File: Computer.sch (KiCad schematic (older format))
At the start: 35 parts, among them J1 DB9, J2 Screw_Terminal_1x04, U1 8284, U10 74LS04, U11 7400, U12 8259, U2 LM2931AZ-5.0, U3 8088, U4 74LS04, U5 28C256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

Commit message: Update to revision A
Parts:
- removed unit 2 of U4
- removed unit 3 of U4
- removed unit 4 of U4
- removed unit 5 of U4
- removed U8: 7400, Housings_DIP:DIP-14_W7.62mm, symbol 7400
- added R16, R17, R4, R5: 10k, Resistors_THT:R_Axial_DIN0204_L3.6mm_D1.6mm_P7.62mm_Horizontal, symbol R
- added unit 6 of U10
- added unit 5 of U10
- added U13, U8: 74LS138, Housings_DIP:DIP-16_W7.62mm, symbol 74LS138
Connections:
- net A0: now also U13.1 (A0), U13.3 (A2)
- net A17: now also U8.1 (A0)
- net A18: now also U8.2 (A1)
- net A19: now also U8.3 (A2)
- net A4: now also U13.2 (A1)
- net GND: now also R16.1, R5.1, U10.7 (GND), U10.7 (GND), U13.8 (GND), U8.8 (GND)
- net IO/M: now also U10.13, U8.5 (E2); no longer U10.3, U10.5, U10.9, U3.32 (~RD~), U5.22 (OE), U6.22 (OE), U7.21 (~RD~)
- net VCC: now also U10.14 (VCC), U10.14 (VCC), U13.16 (VCC), U8.16 (VCC)
- net Vcc: now also R17.2, R4.1
- net WR: now also U10.11
- net at U5.20 (CS): now also U8.7 (O7); no longer U5.27 (WE)
- net at U6.20 (CS): now also U8.15 (O0)
- net at U7.14 (~CS2~): now also U13.15 (O0)
- net at R11.1: now also U5.27 (WE)
- new net: U10.8, U7.21 (~RD~)
- new net: U12.1 (~CS~), U13.14 (O1)
- new net: U10.10, U12.3 (~WR~)
- new net: R5.2, U8.4 (E1)
- new net: R4.2, U8.6 (E3)
- new net: U10.12, U13.4 (E1)
- new net: R16.2, U13.5 (E2)
- new net: R17.1, U13.6 (E3)
- new net RD: U10.3, U10.5, U10.9, U12.2 (~RD~), U3.32 (~RD~), U5.22 (OE), U6.22 (OE)
- no-connect marks 32 -> 44

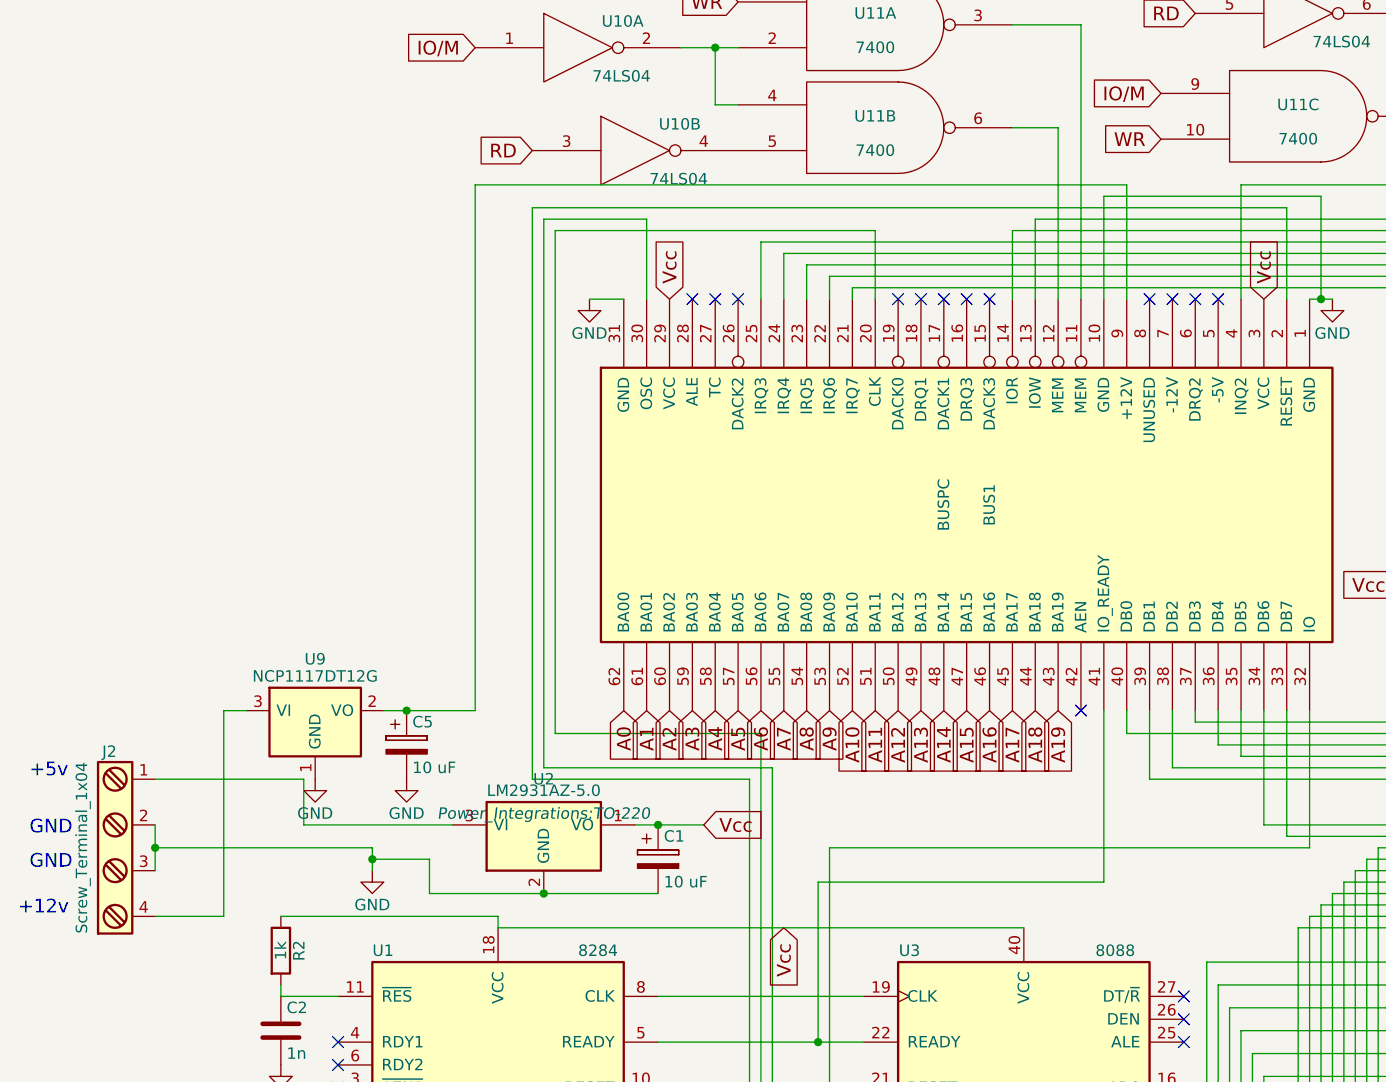
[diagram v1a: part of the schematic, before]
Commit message: Add -12v and -5v rails
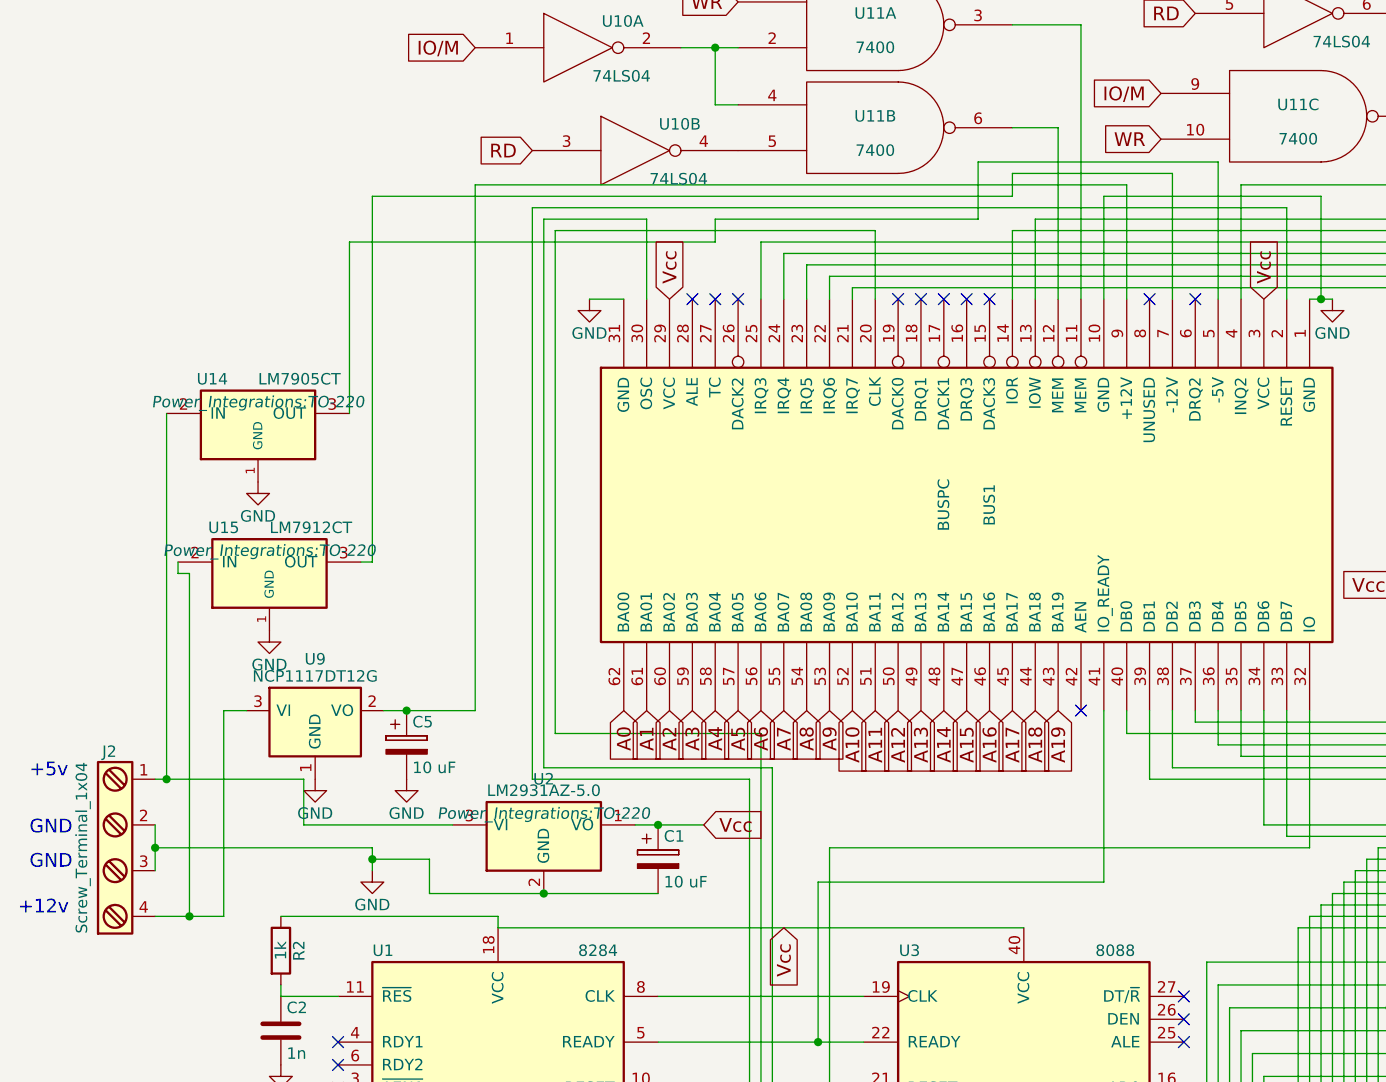
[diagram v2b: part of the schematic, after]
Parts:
- added U14: LM7905CT, Power_Integrations:TO-220, symbol LM7905CT
- added U15: LM7912CT, Power_Integrations:TO-220, symbol LM7912CT
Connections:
- net GND: now also U14.1 (GND), U15.1 (GND)
- net at J2.1, U2.3 (VI): now also U14.2 (IN)
- net at BUS1.5 (-5V): now also U14.3 (OUT)
- net at BUS1.7 (-12V): now also U15.3 (OUT)
- net at J2.4, U9.3 (VI): now also U15.2 (IN)
- no-connect marks 44 -> 42
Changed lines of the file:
@@
 $EndDescr
 $Comp
-L GND #PWR4
+L GND #PWR6
 U 1 1 5887F82B
 P 2300 4700
-F 0 "#PWR4" H 2300 4450 50  0001 C CNN
+F 0 "#PWR6" H 2300 4450 50  0001 C CNN
 F 1 "GND" H 2300 4550 50  0000 C CNN
 F 2 "" H 2300 4700 50  0000 C CNN
@@
 $EndComp
 $Comp
-L GND #PWR9
+L GND #PWR11
 U 1 1 58881BF2
 P 4000 8700
-F 0 "#PWR9" H 4000 8450 50  0001 C CNN
+F 0 "#PWR11" H 4000 8450 50  0001 C CNN
 F 1 "GND" H 4000 8550 50  0000 C CNN
 F 2 "" H 4000 8700 50  0000 C CNN
@@
 $EndComp
 $Comp
-L GND #PWR2
+L GND #PWR4
 U 1 1 58888005
 P 1900 5550
-F 0 "#PWR2" H 1900 5300 50  0001 C CNN
+F 0 "#PWR4" H 1900 5300 50  0001 C CNN
 F 1 "GND" H 1900 5400 50  0000 C CNN
 F 2 "" H 1900 5550 50  0000 C CNN
@@
 $EndComp
 $Comp
-L GND #PWR14
+L GND #PWR16
 U 1 1 588F1D61
 P 10100 8150
-F 0 "#PWR14" H 10100 7900 50  0001 C CNN
+F 0 "#PWR16" H 10100 7900 50  0001 C CNN
 F 1 "GND" H 10100 8000 50  0000 C CNN
 F 2 "" H 10100 8150 50  0000 C CNN
@@
 $EndComp
 $Comp
-L GND #PWR12
+L GND #PWR14
 U 1 1 588F745E
 P 8950 8300
-F 0 "#PWR12" H 8950 8050 50  0001 C CNN
+F 0 "#PWR14" H 8950 8050 50  0001 C CNN
 F 1 "GND" H 8950 8150 50  0000 C CNN
 F 2 "" H 8950 8300 50  0000 C CNN
@@
 $EndComp
 $Comp
-L GND #PWR7
+L GND #PWR9
 U 1 1 588FA3EB
 P 3000 10650
-F 0 "#PWR7" H 3000 10400 50  0001 C CNN
+F 0 "#PWR9" H 3000 10400 50  0001 C CNN
 F 1 "GND" H 3000 10500 50  0000 C CNN
 F 2 "" H 3000 10650 50  0000 C CNN
@@
 $EndComp
 $Comp
-L GND #PWR6
+L GND #PWR8
 U 1 1 588FA459
 P 2700 10650
-F 0 "#PWR6" H 2700 10400 50  0001 C CNN
+F 0 "#PWR8" H 2700 10400 50  0001 C CNN
 F 1 "GND" H 2700 10500 50  0000 C CNN
 F 2 "" H 2700 10650 50  0000 C CNN
@@
 IRQ0
 $Comp
-L GND #PWR13
+L GND #PWR15
 U 1 1 58A2012A
 P 9000 3450
-F 0 "#PWR13" H 9000 3200 50  0001 C CNN
+F 0 "#PWR15" H 9000 3200 50  0001 C CNN
 F 1 "GND" H 9000 3300 50  0000 C CNN
 F 2 "" H 9000 3450 50  0000 C CNN
@@
 NoConn ~ 5700 2200
 $Comp
-L GND #PWR11
+L GND #PWR13
 U 1 1 58A30571
 P 6500 2200
-F 0 "#PWR11" H 6500 1950 50  0001 C CNN
+F 0 "#PWR13" H 6500 1950 50  0001 C CNN
 F 1 "GND" H 6500 2050 50  0000 C CNN
 F 2 "" H 6500 2200 50  0000 C CNN
@@
 $EndComp
 $Comp
-L GND #PWR8
+L GND #PWR10
 U 1 1 58A305FA
 P 3250 2200
-F 0 "#PWR8" H 3250 1950 50  0001 C CNN
+F 0 "#PWR10" H 3250 1950 50  0001 C CNN
 F 1 "GND" H 3250 2050 50  0000 C CNN
 F 2 "" H 3250 2200 50  0000 C CNN
@@
 +12v
 $Comp
-L GND #PWR3
+L GND #PWR5
 U 1 1 58A3B81F
 P 2050 4300
-F 0 "#PWR3" H 2050 4050 50  0001 C CNN
+F 0 "#PWR5" H 2050 4050 50  0001 C CNN
 F 1 "GND" H 2050 4150 50  0000 C CNN
 F 2 "" H 2050 4300 50  0000 C CNN
@@
 $EndComp
 $Comp
-L GND #PWR5
+L GND #PWR7
 U 1 1 58A3B97D
 P 2450 4300
-F 0 "#PWR5" H 2450 4050 50  0001 C CNN
+F 0 "#PWR7" H 2450 4050 50  0001 C CNN
 F 1 "GND" H 2450 4150 50  0000 C CNN
 F 2 "" H 2450 4300 50  0000 C CNN
@@
 	1    0    0    -1
 $EndComp
-NoConn ~ 5800 2200
-NoConn ~ 6000 2200
 NoConn ~ 5900 2200
 NoConn ~ 5000 2200
@@
 IO/M
 $Comp
-L GND #PWR10
+L GND #PWR12
 U 1 1 58C8EE59
 P 4150 10000
-F 0 "#PWR10" H 4150 9750 50  0001 C CNN
+F 0 "#PWR12" H 4150 9750 50  0001 C CNN
 F 1 "GND" H 4150 9850 50  0000 C CNN
 F 2 "" H 4150 10000 50  0000 C CNN
@@
 $EndComp
 $Comp
-L GND #PWR15
+L GND #PWR17
 U 1 1 58C92558
 P 10450 4100
-F 0 "#PWR15" H 10450 3850 50  0001 C CNN
+F 0 "#PWR17" H 10450 3850 50  0001 C CNN
 F 1 "GND" H 10450 3950 50  0000 C CNN
 F 2 "" H 10450 4100 50  0000 C CNN
@@
 Text GLabel 8300 4050 3    60   Input ~ 0
 RD
+Wire Wire Line
+	1500 4900 1500 3400
+Wire Wire Line
+	1500 3400 1450 3400
+Wire Wire Line
+	1450 3400 1450 3350
+Connection ~ 1500 4900
+$Comp
+L GND #PWR3
+U 1 1 58C76930
+P 1850 3650
+F 0 "#PWR3" H 1850 3400 50  0001 C CNN
+F 1 "GND" H 1850 3500 50  0000 C CNN
+F 2 "" H 1850 3650 50  0000 C CNN
+F 3 "" H 1850 3650 50  0000 C CNN
+	1    1850 3650
+	1    0    0    -1
+$EndComp
+$Comp
+L LM7912CT U15
+U 1 1 58C76B56
+P 1850 3400
+F 0 "U15" H 1650 3200 50  0000 C CNN
+F 1 "LM7912CT" H 1850 3200 50  0000 L CNN
+F 2 "Power_Integrations:TO-220" H 1850 3300 50  0000 C CIN
+F 3 "" H 1850 3400 50  0000 C CNN
+	1    1850 3400
+	1    0    0    1
+$EndComp
+Wire Wire Line
+	5800 2200 5800 1650
+Wire Wire Line
+	5800 1650 5100 1650
+Wire Wire Line
+	5100 1650 5100 1750
+Wire Wire Line
+	5100 1750 2300 1750
+Wire Wire Line
+	2300 1750 2300 3350
+Wire Wire Line
+	2300 3350 2250 3350
+$Comp
+L LM7905CT U14
+U 1 1 58C76E6A
+P 1800 2750
+F 0 "U14" H 1600 2550 50  0000 C CNN
+F 1 "LM7905CT" H 1800 2550 50  0000 L CNN
+F 2 "Power_Integrations:TO-220" H 1800 2650 50  0000 C CIN
+F 3 "" H 1800 2750 50  0000 C CNN
+	1    1800 2750
+	1    0    0    1
+$EndComp
+Wire Wire Line
+	1400 4300 1400 2700
+Connection ~ 1400 4300
+$Comp
+L GND #PWR2
+U 1 1 58C7715E
+P 1800 3000
+F 0 "#PWR2" H 1800 2750 50  0001 C CNN
+F 1 "GND" H 1800 2850 50  0000 C CNN
+F 2 "" H 1800 3000 50  0000 C CNN
+F 3 "" H 1800 3000 50  0000 C CNN
+	1    1800 3000
+	1    0    0    -1
+$EndComp
+Wire Wire Line
+	6000 2200 6000 1600
+Wire Wire Line
+	6000 1600 4950 1600
+Wire Wire Line
+	4950 1600 4950 1850
+Wire Wire Line
+	4950 1850 3800 1850
+Wire Wire Line
+	3800 1850 3800 1950
+Wire Wire Line
+	3800 1950 2200 1950
+Wire Wire Line
+	2200 1950 2200 2700
 $EndSCHEMATC
